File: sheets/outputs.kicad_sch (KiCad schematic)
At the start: 1 part, among them U20 ULN2803A

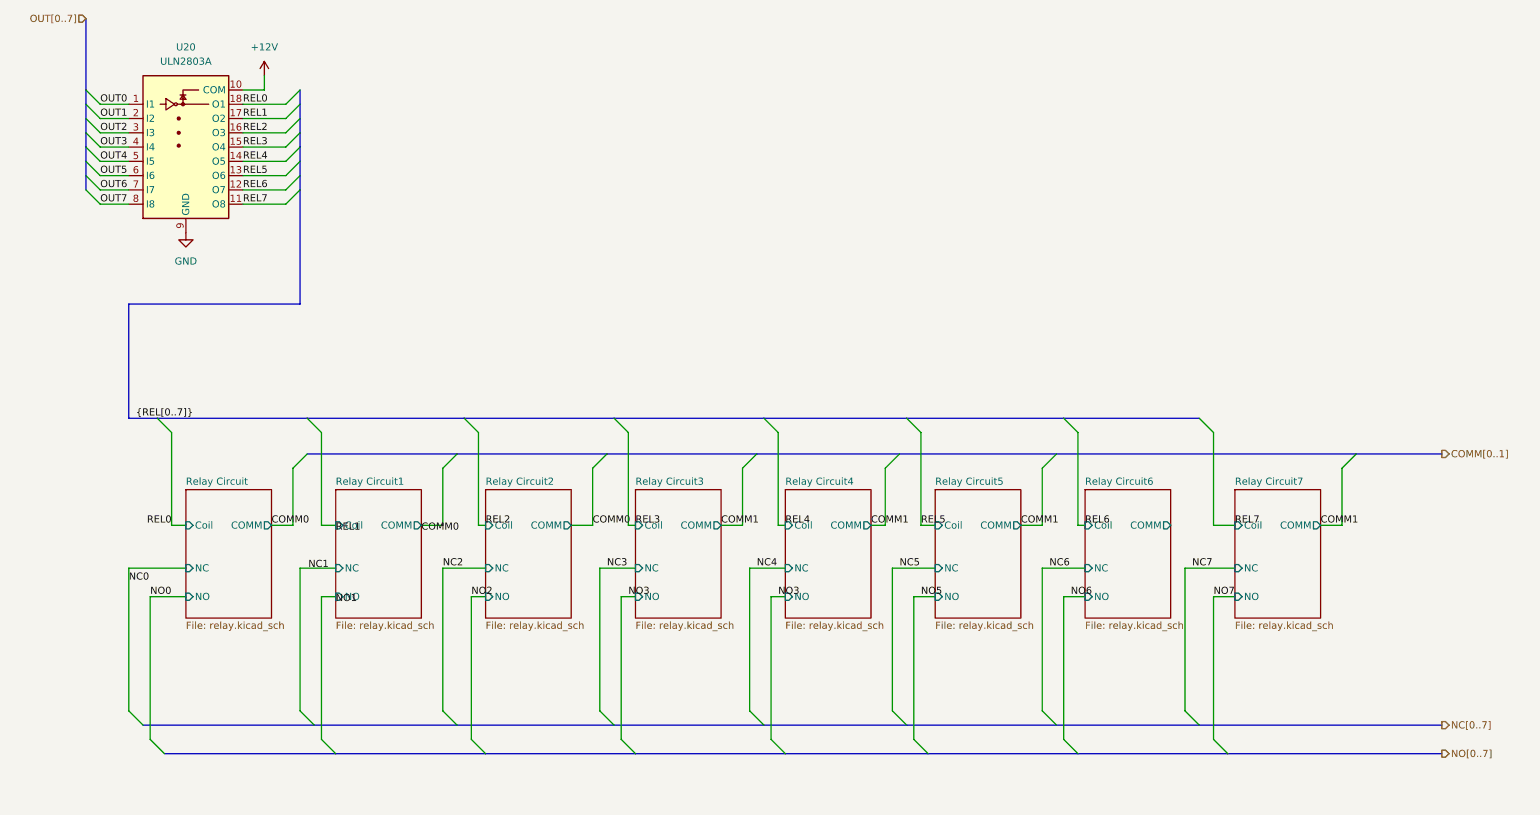
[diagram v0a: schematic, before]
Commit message: add mcu module + position components
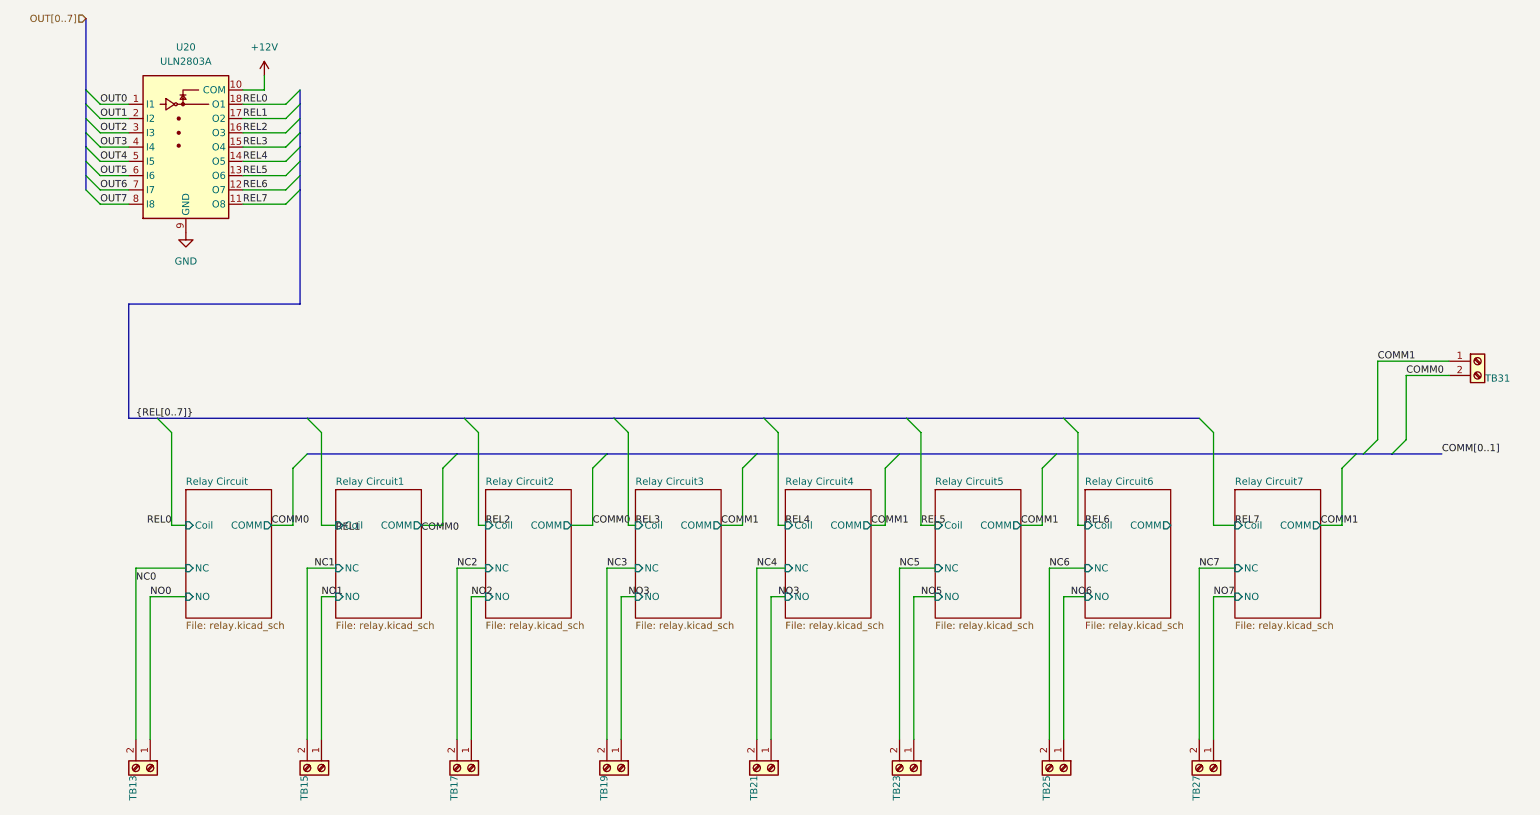
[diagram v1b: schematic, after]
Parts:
- added TB13, TB15, TB17, TB19, TB21, TB23, TB25, TB27, TB31: MKDSN 1,5/ 2-5,08, TerminalBlock_Phoenix:TerminalBlock_Phoenix_MKDS-1,5-2-5.08_1x02_P5.08mm_Horizontal, symbol Connector:Screw_Terminal_01x02
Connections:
- net COMM0: now also TB31.2 (Pin_2)
- net COMM1: now also TB31.1 (Pin_1)
- net NC0: now also TB13.2 (Pin_2)
- net NC1: now also TB15.2 (Pin_2)
- net NC2: now also TB17.2 (Pin_2)
- net NC3: now also TB19.2 (Pin_2)
- net NC4: now also TB21.2 (Pin_2)
- net NC5: now also TB23.2 (Pin_2)
- net NC6: now also TB25.2 (Pin_2)
- net NC7: now also TB27.2 (Pin_2)
- net NO0: now also TB13.1 (Pin_1)
- net NO1: now also TB15.1 (Pin_1)
- net NO2: now also TB17.1 (Pin_1)
- net NO3: now also TB19.1 (Pin_1), TB21.1 (Pin_1)
- net NO5: now also TB23.1 (Pin_1)
- net NO6: now also TB25.1 (Pin_1)
- net NO7: now also TB27.1 (Pin_1)
